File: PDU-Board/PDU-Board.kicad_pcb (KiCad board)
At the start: 2 copper layers, 180 x 93 mm, 12 parts, among them J0 Main Feed, J1 Motor-1, J2 Motor-2, J3 Mother Board, J4 RJ45, J5 RJ45, U1 VICOR-DC-DC, U2 VICOR-DC-DC, U3 VICOR-DC-DC, U4 VICOR-DC-DC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

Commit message: PDU updated
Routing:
- added copper zone on B.Cu, net +48V
- added copper zone on F.Cu, net 48v_GND
- removed copper zone on F.Cu, net +48V
- removed copper zone on B.Cu, net 48v_GND
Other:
- board size 180 x 93 mm -> 180 x 88 mm
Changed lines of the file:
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@@
     )
   )
-  (gr_line (start 95 80) (end 275 80) (angle 90) (layer Edge.Cuts) (width 0.2))
-  (gr_line (start 275 173) (end 95 173) (angle 90) (layer Edge.Cuts) (width 0.2))
+  (gr_line (start 95 83) (end 275 83) (angle 90) (layer Edge.Cuts) (width 0.2))
+  (gr_line (start 95 171) (end 95 83) (angle 90) (layer Edge.Cuts) (width 0.2))
+  (gr_line (start 275 171) (end 95 171) (angle 90) (layer Edge.Cuts) (width 0.2))
+  (gr_line (start 275 83) (end 275 171) (angle 90) (layer Edge.Cuts) (width 0.2))
   (gr_text "Airzona State Underwater Robotics PDU 2019 rev.0\n" (at 186 99.2) (layer F.SilkS)
     (effects (font (size 1.5 1.5) (thickness 0.3)))
@@
     (effects (font (size 1.5 1.5) (thickness 0.3)) (justify mirror))
   )
-  (gr_line (start 275 173) (end 275 80) (layer Edge.Cuts) (width 0.2))
-  (gr_line (start 95 80) (end 95 173) (layer Edge.Cuts) (width 0.2))
   (segment (start 183.04 125.5) (end 183.04 106) (width 0.1524) (layer F.Cu) (net 4) (status C00000))
   (segment (start 186.85 122.96) (end 186.85 103.46) (width 0.1524) (layer F.Cu) (net 7) (status C00000))
@@
     (polygon
       (pts
-        (xy 275 173) (xy 275 119) (xy 95 119) (xy 95 173)
+        (xy 275 171) (xy 275 121) (xy 95 121) (xy 95 171)
       )
     )
@@
     (polygon
       (pts
-        (xy 275 173) (xy 275 119) (xy 95 119) (xy 95 173)
+        (xy 275 171) (xy 275 121) (xy 95 121) (xy 95 171)
       )
     )
   )
-  (zone (net 2) (net_name 48v_GND) (layer B.Cu) (hatch edge 0.508)
+  (zone (net 2) (net_name 48v_GND) (layer F.Cu) (hatch edge 0.508)
     (connect_pads yes (clearance 0.508))
     (min_thickness 0.254)
@@
     (polygon
       (pts
-        (xy 275 108) (xy 95 108) (xy 95 80) (xy 275 80)
+        (xy 275 83) (xy 275 99) (xy 275 102) (xy 275 106) (xy 132 106)
+        (xy 95 106) (xy 95 83)
       )
     )
   )
-  (zone (net 1) (net_name +48V) (layer F.Cu) (hatch edge 0.508)
+  (zone (net 1) (net_name +48V) (layer B.Cu) (hatch edge 0.508)
     (connect_pads yes (clearance 0.508))
     (min_thickness 0.254)
@@
     (polygon
       (pts
-        (xy 275 108) (xy 95 108) (xy 95 80) (xy 275 80)
+        (xy 275 83) (xy 275 106) (xy 95 106) (xy 95 83)
       )
     )

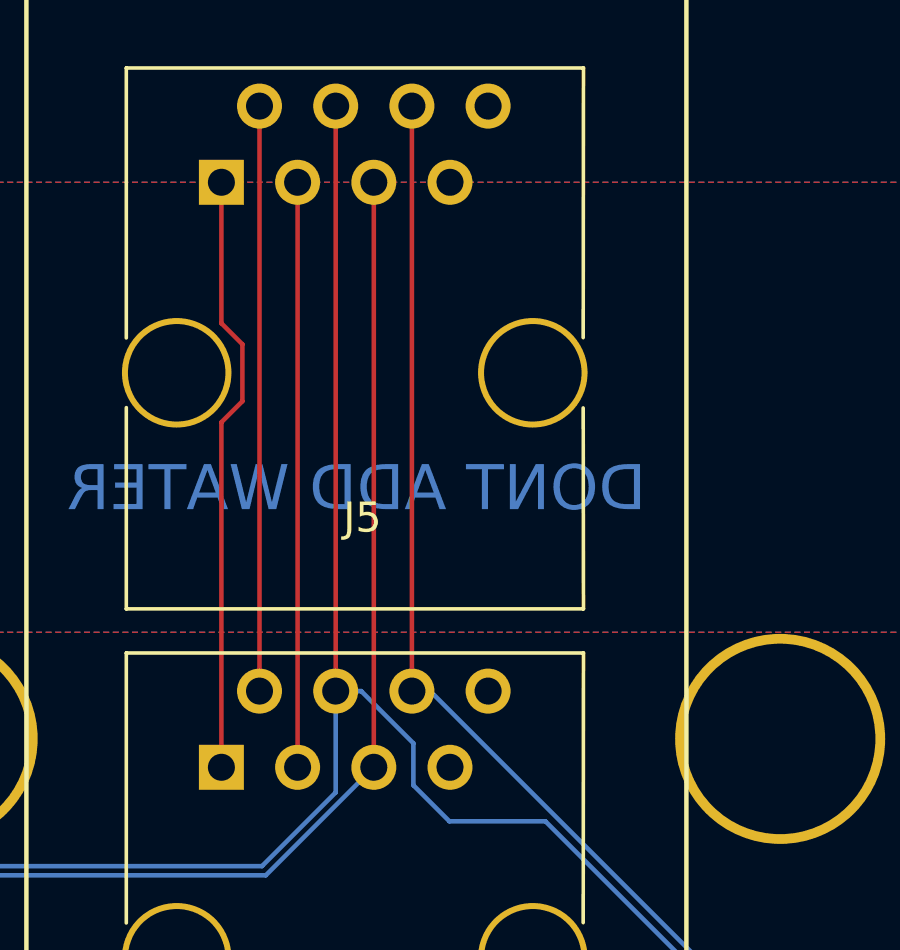
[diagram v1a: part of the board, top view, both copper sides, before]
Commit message: Updated PDU and ESC for leak sensor
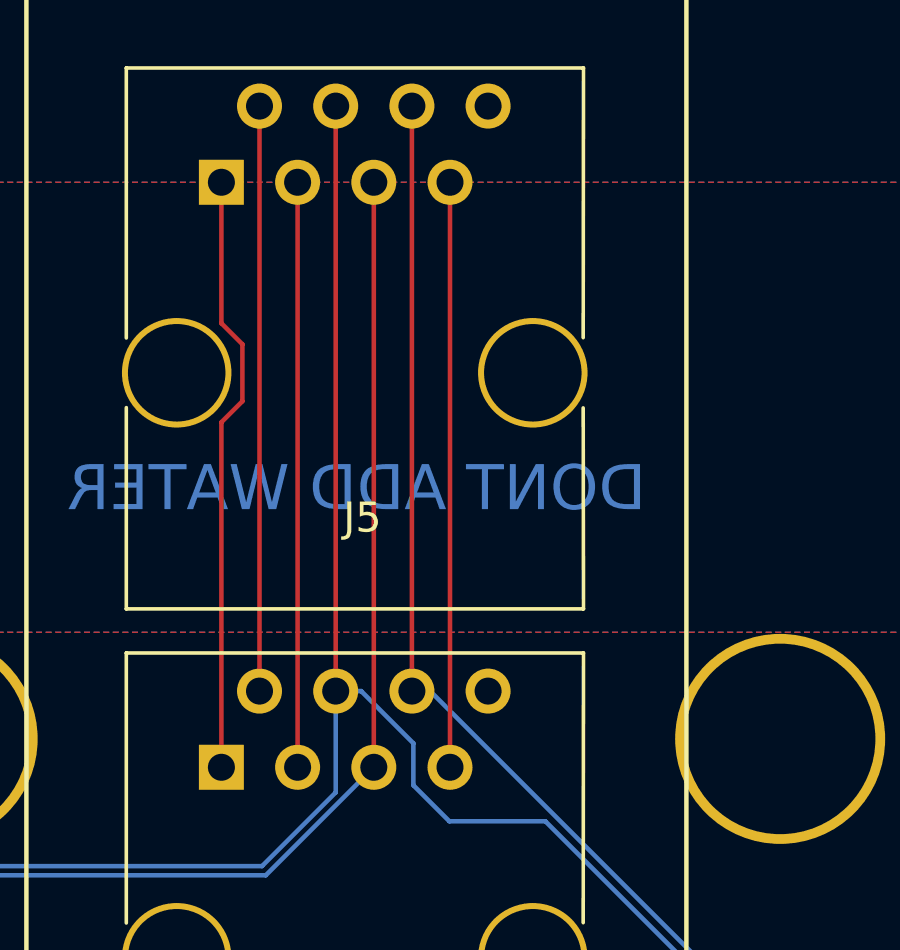
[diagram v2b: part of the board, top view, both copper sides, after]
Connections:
- J4 pad 7: Net-(J4-Pad7) -> Water_Sensor
- J5 pad 7: Net-(J5-Pad7) -> Water_Sensor
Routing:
- net Water_Sensor: track 0.00 -> 19.5 mm

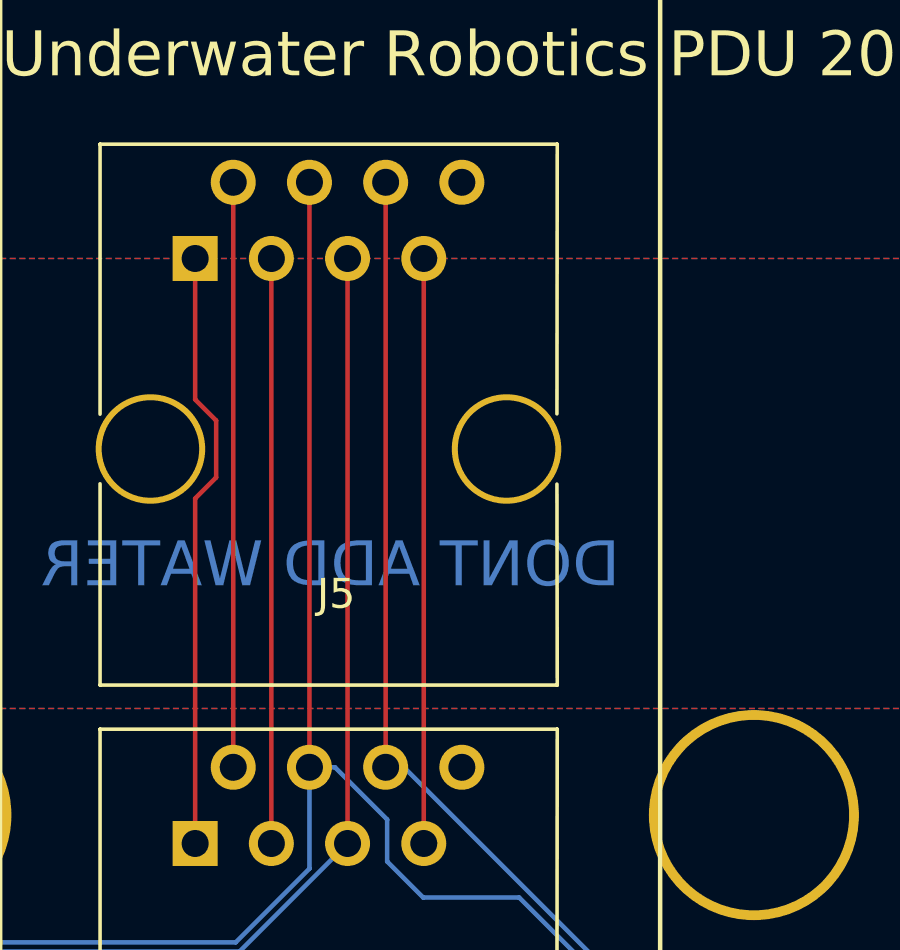
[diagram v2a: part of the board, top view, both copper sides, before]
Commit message: Added 5v
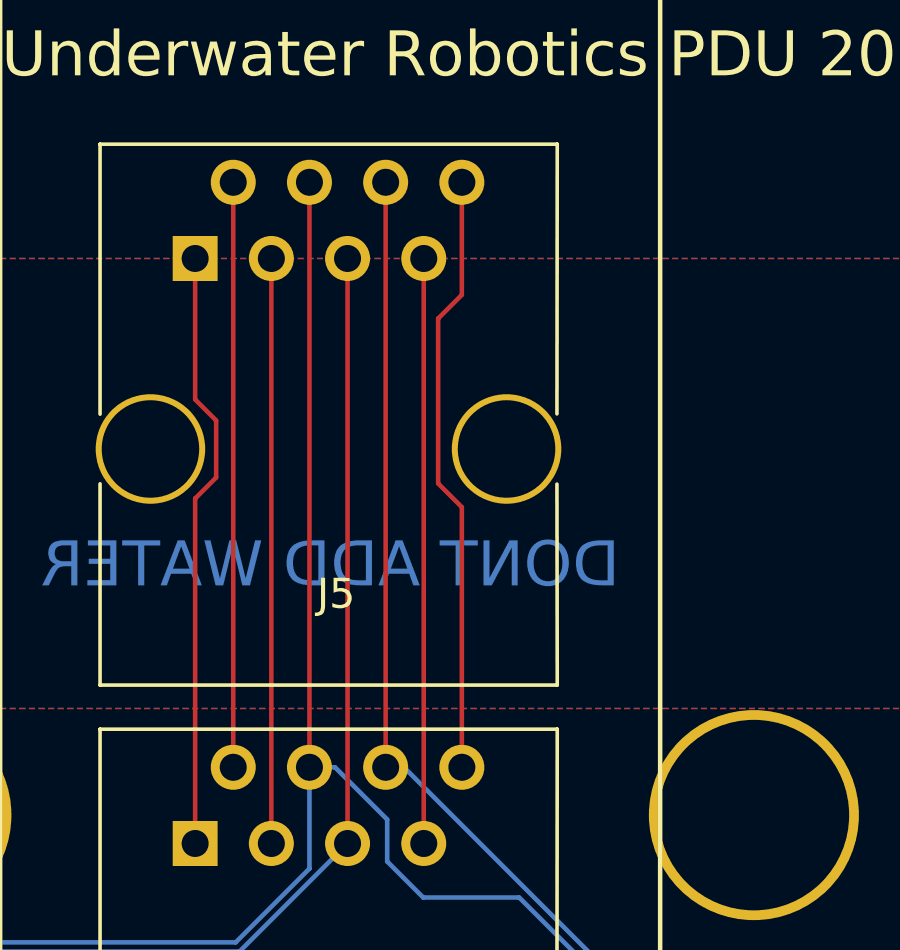
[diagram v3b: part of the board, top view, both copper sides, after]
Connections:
- J5 pad 8: Net-(J5-Pad8) -> Net-(J4-Pad8)
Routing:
- net Net-(J4-Pad8): track 0.00 -> 20.2 mm
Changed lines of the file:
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@@
     (thickness 1.6)
     (drawings 6)
-    (tracks 31)
+    (tracks 36)
     (zones 0)
     (modules 12)
-    (nets 13)
+    (nets 12)
   )
   (page A3)
@@
   (net 9 "Net-(J4-Pad2)")
   (net 10 "Net-(J4-Pad1)")
-  (net 11 "Net-(J5-Pad8)")
-  (net 12 Water_Sensor)
+  (net 11 Water_Sensor)
   (net_class Default "This is the default net class."
     (clearance 0.1524)
@@
     (add_net "Net-(J4-Pad2)")
     (add_net "Net-(J4-Pad8)")
-    (add_net "Net-(J5-Pad8)")
     (add_net Water_Sensor)
   )
@@
       (net 5 "Net-(J4-Pad8)"))
     (pad 7 thru_hole circle (at 7.62 0) (size 1.5 1.5) (drill 0.9) (layers *.Cu *.Mask)
-      (net 12 Water_Sensor))
+      (net 11 Water_Sensor))
     (pad 6 thru_hole circle (at 6.35 -2.54) (size 1.5 1.5) (drill 0.9) (layers *.Cu *.Mask)
       (net 6 Ext_Temp_1))
@@
     (fp_line (start -3.17 14.22) (end 12.07 14.22) (layer F.SilkS) (width 0.12))
     (pad 8 thru_hole circle (at 8.89 -2.54) (size 1.5 1.5) (drill 0.9) (layers *.Cu *.Mask)
-      (net 11 "Net-(J5-Pad8)"))
+      (net 5 "Net-(J4-Pad8)"))
     (pad 7 thru_hole circle (at 7.62 0) (size 1.5 1.5) (drill 0.9) (layers *.Cu *.Mask)
-      (net 12 Water_Sensor))
+      (net 11 Water_Sensor))
     (pad 6 thru_hole circle (at 6.35 -2.54) (size 1.5 1.5) (drill 0.9) (layers *.Cu *.Mask)
       (net 6 Ext_Temp_1))
@@
   )
   (segment (start 183.04 125.5) (end 183.04 106) (width 0.1524) (layer F.Cu) (net 4) (status C00000))
+  (segment (start 189.39 122.96) (end 189.39 114.29) (width 0.1524) (layer F.Cu) (net 5) (status 400000))
+  (segment (start 189.39 107.21) (end 189.39 103.46) (width 0.1524) (layer F.Cu) (net 5) (status 800000))
+  (segment (start 188.6 108) (end 189.39 107.21) (width 0.1524) (layer F.Cu) (net 5))
+  (segment (start 188.6 113.5) (end 188.6 108) (width 0.1524) (layer F.Cu) (net 5))
+  (segment (start 189.39 114.29) (end 188.6 113.5) (width 0.1524) (layer F.Cu) (net 5))
   (segment (start 186.85 122.96) (end 186.85 103.46) (width 0.1524) (layer F.Cu) (net 6) (status C00000))
   (segment (start 187.5 123) (end 198.1 133.6) (width 0.1524) (layer B.Cu) (net 6) (status 400000))
@@
   (segment (start 181.2 113.3) (end 181.2 111.4) (width 0.1524) (layer F.Cu) (net 10))
   (segment (start 180.5 114) (end 181.2 113.3) (width 0.1524) (layer F.Cu) (net 10))
-  (segment (start 188.12 125.5) (end 188.12 106) (width 0.1524) (layer F.Cu) (net 12) (status C00000))
+  (segment (start 188.12 125.5) (end 188.12 106) (width 0.1524) (layer F.Cu) (net 11) (status C00000))
   (zone (net 3) (net_name +12V) (layer F.Cu) (hatch edge 0.508)
     (connect_pads yes (clearance 0.508))
